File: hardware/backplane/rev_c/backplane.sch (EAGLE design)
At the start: 377 parts, among them J0 BACKPLANE_GENERIC_MODULE, J1 BACKPLANE_GENERIC_MODULE, J2 BACKPLANE_GENERIC_MODULE, J3 BACKPLANE_CONTROLLER_MODULE, J4 BACKPLANE_POWER_MODULE, J5 BACKPLANE_GENERIC_MODULE, J6 BACKPLANE_GENERIC_MODULE, J7 BACKPLANE_GENERIC_MODULE, U1 TUSB2077A, U10 SN74LVC2T45, U11 SN74LVC2T45, U12 SN74LVC2T45, U13 SN74LVC2T45, U14 SN74LVC2T45, U15 SN74LVC2T45, U16 SN74LVC2T45, U17 SN74LVC2T45, U18 SN74LVC2T45, U19 SN74LVC2T45, U2 FXMA2102, U20 TS3USB30E, U21 TS3USB30E, U22 TS3USB30E, U23 TS3USB30E, U24 TS3USB30E, U25 TS3USB30E, U26 MCP23008, U27 MCP23008, U28 MCP23008, U29 MCP23008, U3 FXMA2102, U30 MCP23008, U31 MCP23008, U4 FXMA2102, U5 FXMA2102, U6 FXMA2102, U7 FXMA2102, U8 SN74LVC2T45, U9 SN74LVC2T45, Y1 ABMM

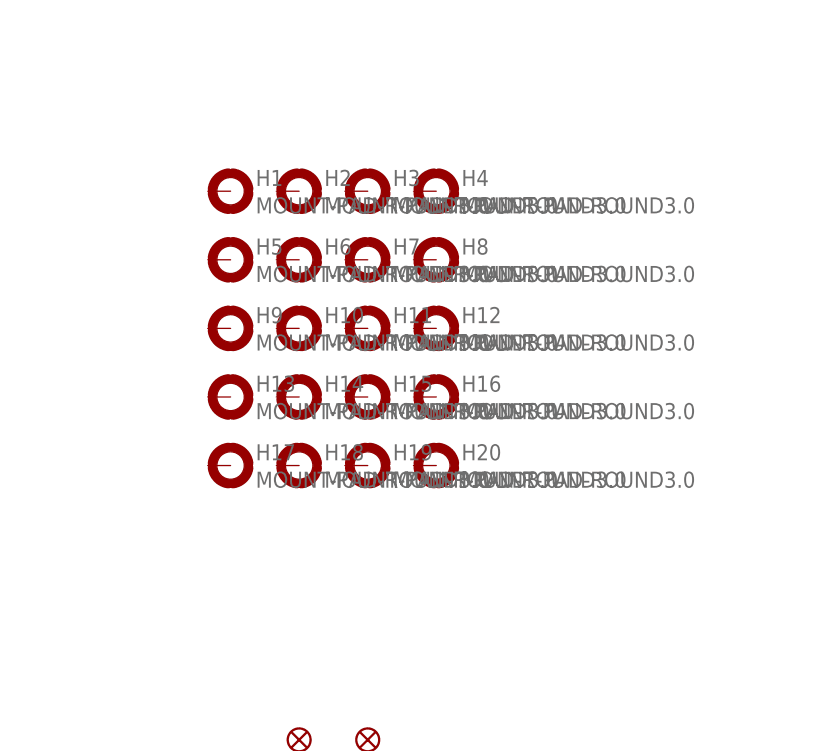
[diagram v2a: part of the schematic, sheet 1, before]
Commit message: backplane: attach mounting holes to GND
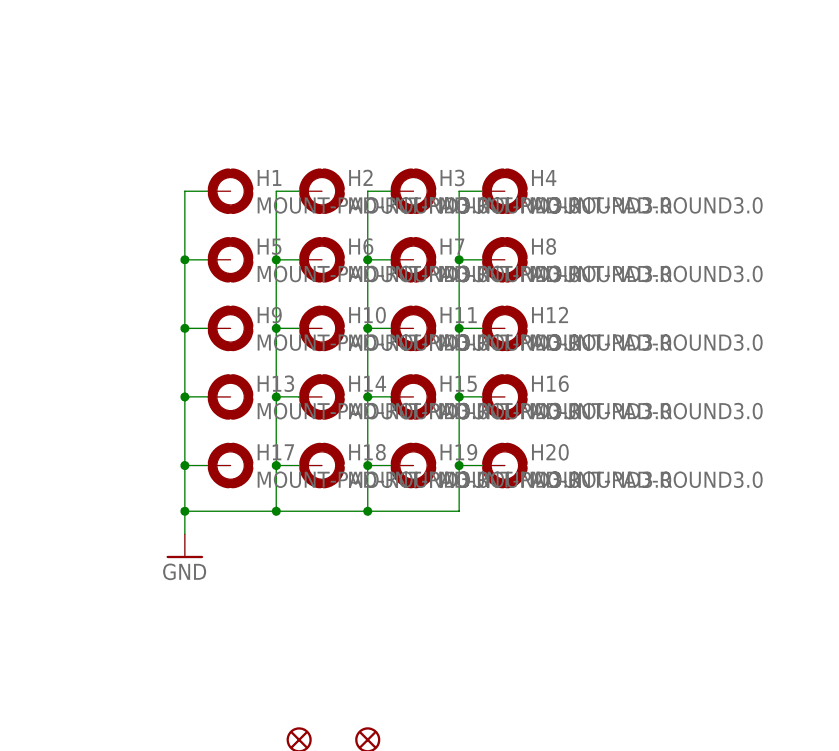
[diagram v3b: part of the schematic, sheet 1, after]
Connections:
- net GND: now also H1.MOUNT, H10.MOUNT, H11.MOUNT, H12.MOUNT, H13.MOUNT, H14.MOUNT, H15.MOUNT, H16.MOUNT, H17.MOUNT, H18.MOUNT, H19.MOUNT, H2.MOUNT, H20.MOUNT, H3.MOUNT, H4.MOUNT, H5.MOUNT, H6.MOUNT, H7.MOUNT, H8.MOUNT, H9.MOUNT
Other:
- moved on the sheet: H10, H11, H12, H14, H15, H16, H18, H19, H2, H20, H3, H4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
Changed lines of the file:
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@@
 <part name="H19" library="holes" deviceset="MOUNT-PAD-ROUND" device="3.0"/>
 <part name="H20" library="holes" deviceset="MOUNT-PAD-ROUND" device="3.0"/>
+<part name="GND72" library="umich" deviceset="GND" device=""/>
 </parts>
 <sheets>
@@
 <text x="246.38" y="182.88" size="5.08" layer="98" align="top-right">Special Modules</text>
 <text x="147.32" y="175.26" size="2.54" layer="98" align="center">Pull-up/downs</text>
-<wire x1="243.84" y1="76.2" x2="203.2" y2="76.2" width="0.6096" layer="98"/>
-<wire x1="203.2" y1="76.2" x2="203.2" y2="20.32" width="0.6096" layer="98"/>
+<wire x1="248.92" y1="76.2" x2="198.12" y2="76.2" width="0.6096" layer="98"/>
+<wire x1="198.12" y1="76.2" x2="198.12" y2="20.32" width="0.6096" layer="98"/>
 <text x="220.98" y="71.12" size="2.54" layer="98" align="center">Fiducials</text>
-<wire x1="203.2" y1="132.08" x2="203.2" y2="76.2" width="0.6096" layer="98"/>
+<wire x1="198.12" y1="132.08" x2="198.12" y2="76.2" width="0.6096" layer="98"/>
 <text x="223.52" y="129.54" size="2.54" layer="98" align="center">Plated Mounting Holes</text>
 </plain>
@@
 <instance part="JP6" gate="G$1" x="223.52" y="40.64"/>
 <instance part="H1" gate="G$1" x="208.28" y="121.92"/>
-<instance part="H2" gate="G$1" x="215.9" y="121.92"/>
-<instance part="H3" gate="G$1" x="223.52" y="121.92"/>
-<instance part="H4" gate="G$1" x="231.14" y="121.92"/>
+<instance part="H2" gate="G$1" x="218.44" y="121.92"/>
+<instance part="H3" gate="G$1" x="228.6" y="121.92"/>
+<instance part="H4" gate="G$1" x="238.76" y="121.92"/>
 <instance part="H5" gate="G$1" x="208.28" y="114.3"/>
-<instance part="H6" gate="G$1" x="215.9" y="114.3"/>
-<instance part="H7" gate="G$1" x="223.52" y="114.3"/>
-<instance part="H8" gate="G$1" x="231.14" y="114.3"/>
+<instance part="H6" gate="G$1" x="218.44" y="114.3"/>
+<instance part="H7" gate="G$1" x="228.6" y="114.3"/>
+<instance part="H8" gate="G$1" x="238.76" y="114.3"/>
 <instance part="H9" gate="G$1" x="208.28" y="106.68"/>
-<instance part="H10" gate="G$1" x="215.9" y="106.68"/>
-<instance part="H11" gate="G$1" x="223.52" y="106.68"/>
-<instance part="H12" gate="G$1" x="231.14" y="106.68"/>
+<instance part="H10" gate="G$1" x="218.44" y="106.68"/>
+<instance part="H11" gate="G$1" x="228.6" y="106.68"/>
+<instance part="H12" gate="G$1" x="238.76" y="106.68"/>
 <instance part="H13" gate="G$1" x="208.28" y="99.06"/>
-<instance part="H14" gate="G$1" x="215.9" y="99.06"/>
-<instance part="H15" gate="G$1" x="223.52" y="99.06"/>
-<instance part="H16" gate="G$1" x="231.14" y="99.06"/>
+<instance part="H14" gate="G$1" x="218.44" y="99.06"/>
+<instance part="H15" gate="G$1" x="228.6" y="99.06"/>
+<instance part="H16" gate="G$1" x="238.76" y="99.06"/>
 <instance part="H17" gate="G$1" x="208.28" y="91.44"/>
-<instance part="H18" gate="G$1" x="215.9" y="91.44"/>
-<instance part="H19" gate="G$1" x="223.52" y="91.44"/>
-<instance part="H20" gate="G$1" x="231.14" y="91.44"/>
+<instance part="H18" gate="G$1" x="218.44" y="91.44"/>
+<instance part="H19" gate="G$1" x="228.6" y="91.44"/>
+<instance part="H20" gate="G$1" x="238.76" y="91.44"/>
+<instance part="GND72" gate="1" x="203.2" y="81.28"/>
 </instances>
 <busses>
@@
 <wire x1="88.9" y1="99.06" x2="88.9" y2="93.98" width="0.1524" layer="91"/>
 </segment>
-</net>
+<segment>
+<pinref part="H17" gate="G$1" pin="MOUNT"/>
+<wire x1="205.74" y1="91.44" x2="203.2" y2="91.44" width="0.1524" layer="91"/>
+<wire x1="203.2" y1="91.44" x2="203.2" y2="86.36" width="0.1524" layer="91"/>
+<pinref part="GND72" gate="1" pin="GND"/>
+<pinref part="H13" gate="G$1" pin="MOUNT"/>
+<wire x1="203.2" y1="86.36" x2="203.2" y2="83.82" width="0.1524" layer="91"/>
+<wire x1="205.74" y1="99.06" x2="203.2" y2="99.06" width="0.1524" layer="91"/>
+<wire x1="203.2" y1="99.06" x2="203.2" y2="91.44" width="0.1524" layer="91"/>
+<junction x="203.2" y="91.44"/>
+<pinref part="H9" gate="G$1" pin="MOUNT"/>
+<wire x1="205.74" y1="106.68" x2="203.2" y2="106.68" width="0.1524" layer="91"/>
+<wire x1="203.2" y1="106.68" x2="203.2" y2="99.06" width="0.1524" layer="91"/>
+<junction x="203.2" y="99.06"/>
+<pinref part="H5" gate="G$1" pin="MOUNT"/>
+<wire x1="205.74" y1="114.3" x2="203.2" y2="114.3" width="0.1524" layer="91"/>
+<wire x1="203.2" y1="114.3" x2="203.2" y2="106.68" width="0.1524" layer="91"/>
+<junction x="203.2" y="106.68"/>
+<pinref part="H1" gate="G$1" pin="MOUNT"/>
+<wire x1="205.74" y1="121.92" x2="203.2" y2="121.92" width="0.1524" layer="91"/>
+<wire x1="203.2" y1="121.92" x2="203.2" y2="114.3" width="0.1524" layer="91"/>
+<junction x="203.2" y="114.3"/>
+<pinref part="H20" gate="G$1" pin="MOUNT"/>
+<wire x1="236.22" y1="91.44" x2="233.68" y2="91.44" width="0.1524" layer="91"/>
+<wire x1="233.68" y1="91.44" x2="233.68" y2="86.36" width="0.1524" layer="91"/>
+<wire x1="233.68" y1="86.36" x2="223.52" y2="86.36" width="0.1524" layer="91"/>
+<junction x="203.2" y="86.36"/>
+<pinref part="H16" gate="G$1" pin="MOUNT"/>
+<wire x1="223.52" y1="86.36" x2="213.36" y2="86.36" width="0.1524" layer="91"/>
+<wire x1="213.36" y1="86.36" x2="203.2" y2="86.36" width="0.1524" layer="91"/>
+<wire x1="236.22" y1="99.06" x2="233.68" y2="99.06" width="0.1524" layer="91"/>
+<wire x1="233.68" y1="99.06" x2="233.68" y2="91.44" width="0.1524" layer="91"/>
+<junction x="233.68" y="91.44"/>
+<pinref part="H12" gate="G$1" pin="MOUNT"/>
+<wire x1="236.22" y1="106.68" x2="233.68" y2="106.68" width="0.1524" layer="91"/>
+<wire x1="233.68" y1="106.68" x2="233.68" y2="99.06" width="0.1524" layer="91"/>
+<junction x="233.68" y="99.06"/>
+<pinref part="H8" gate="G$1" pin="MOUNT"/>
+<wire x1="236.22" y1="114.3" x2="233.68" y2="114.3" width="0.1524" layer="91"/>
+<wire x1="233.68" y1="114.3" x2="233.68" y2="106.68" width="0.1524" layer="91"/>
+<junction x="233.68" y="106.68"/>
+<pinref part="H4" gate="G$1" pin="MOUNT"/>
+<wire x1="236.22" y1="121.92" x2="233.68" y2="121.92" width="0.1524" layer="91"/>
+<wire x1="233.68" y1="121.92" x2="233.68" y2="114.3" width="0.1524" layer="91"/>
+<junction x="233.68" y="114.3"/>
+<pinref part="H18" gate="G$1" pin="MOUNT"/>
+<wire x1="215.9" y1="91.44" x2="213.36" y2="91.44" width="0.1524" layer="91"/>
+<wire x1="213.36" y1="91.44" x2="213.36" y2="86.36" width="0.1524" layer="91"/>
+<junction x="213.36" y="86.36"/>
+<pinref part="H14" gate="G$1" pin="MOUNT"/>
+<wire x1="215.9" y1="99.06" x2="213.36" y2="99.06" width="0.1524" layer="91"/>
+<wire x1="213.36" y1="99.06" x2="213.36" y2="91.44" width="0.1524" layer="91"/>
+<junction x="213.36" y="91.44"/>
+<pinref part="H10" gate="G$1" pin="MOUNT"/>
+<wire x1="215.9" y1="106.68" x2="213.36" y2="106.68" width="0.1524" layer="91"/>
+<wire x1="213.36" y1="106.68" x2="213.36" y2="99.06" width="0.1524" layer="91"/>
+<junction x="213.36" y="99.06"/>
+<pinref part="H6" gate="G$1" pin="MOUNT"/>
+<wire x1="215.9" y1="114.3" x2="213.36" y2="114.3" width="0.1524" layer="91"/>
+<wire x1="213.36" y1="114.3" x2="213.36" y2="106.68" width="0.1524" layer="91"/>
+<junction x="213.36" y="106.68"/>
+<pinref part="H2" gate="G$1" pin="MOUNT"/>
+<wire x1="215.9" y1="121.92" x2="213.36" y2="121.92" width="0.1524" layer="91"/>
+<wire x1="213.36" y1="121.92" x2="213.36" y2="114.3" width="0.1524" layer="91"/>
+<junction x="213.36" y="114.3"/>
+<pinref part="H19" gate="G$1" pin="MOUNT"/>
+<wire x1="226.06" y1="91.44" x2="223.52" y2="91.44" width="0.1524" layer="91"/>
+<wire x1="223.52" y1="91.44" x2="223.52" y2="86.36" width="0.1524" layer="91"/>
+<junction x="223.52" y="86.36"/>
+<pinref part="H15" gate="G$1" pin="MOUNT"/>
+<wire x1="226.06" y1="99.06" x2="223.52" y2="99.06" width="0.1524" layer="91"/>
+<wire x1="223.52" y1="99.06" x2="223.52" y2="91.44" width="0.1524" layer="91"/>
+<junction x="223.52" y="91.44"/>
+<pinref part="H11" gate="G$1" pin="MOUNT"/>
+<wire x1="226.06" y1="106.68" x2="223.52" y2="106.68" width="0.1524" layer="91"/>
+<wire x1="223.52" y1="106.68" x2="223.52" y2="99.06" width="0.1524" layer="91"/>
+<junction x="223.52" y="99.06"/>
+<pinref part="H7" gate="G$1" pin="MOUNT"/>
+<wire x1="226.06" y1="114.3" x2="223.52" y2="114.3" width="0.1524" layer="91"/>
+<wire x1="223.52" y1="114.3" x2="223.52" y2="106.68" width="0.1524" layer="91"/>
+<junction x="223.52" y="106.68"/>
+<pinref part="H3" gate="G$1" pin="MOUNT"/>
+<wire x1="226.06" y1="121.92" x2="223.52" y2="121.92" width="0.1524" layer="91"/>
+<wire x1="223.52" y1="121.92" x2="223.52" y2="114.3" width="0.1524" layer="91"/>
+<junction x="223.52" y="114.3"/>
+</segment>
+</net>

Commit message: backplane: smaller gpio extender package
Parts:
- U26, U27, U28, U29, U30, U31: value MCP23008 -> MCP23008QFN; device signpost:MCP23008 -> signpost:MCP23008QFN
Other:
- moved on the sheet: U26, U27, U28, U29, U30, U31

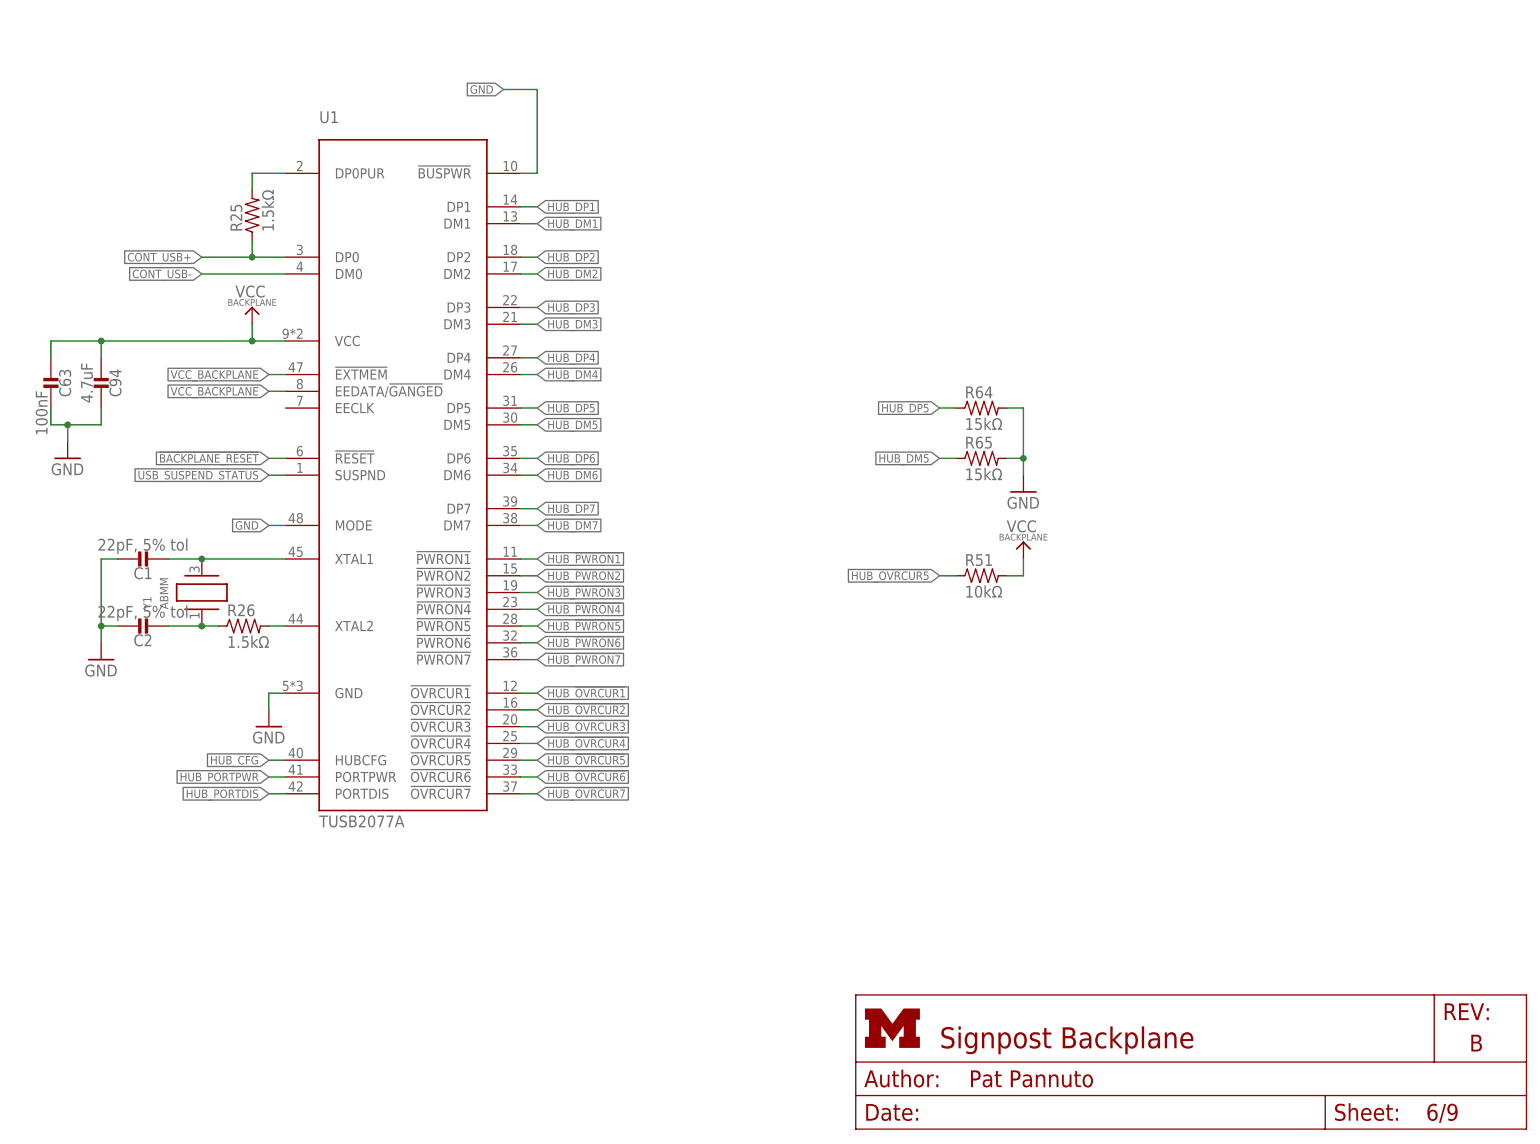
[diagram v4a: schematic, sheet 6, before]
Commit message: backplane: add gpio extender for usb signals
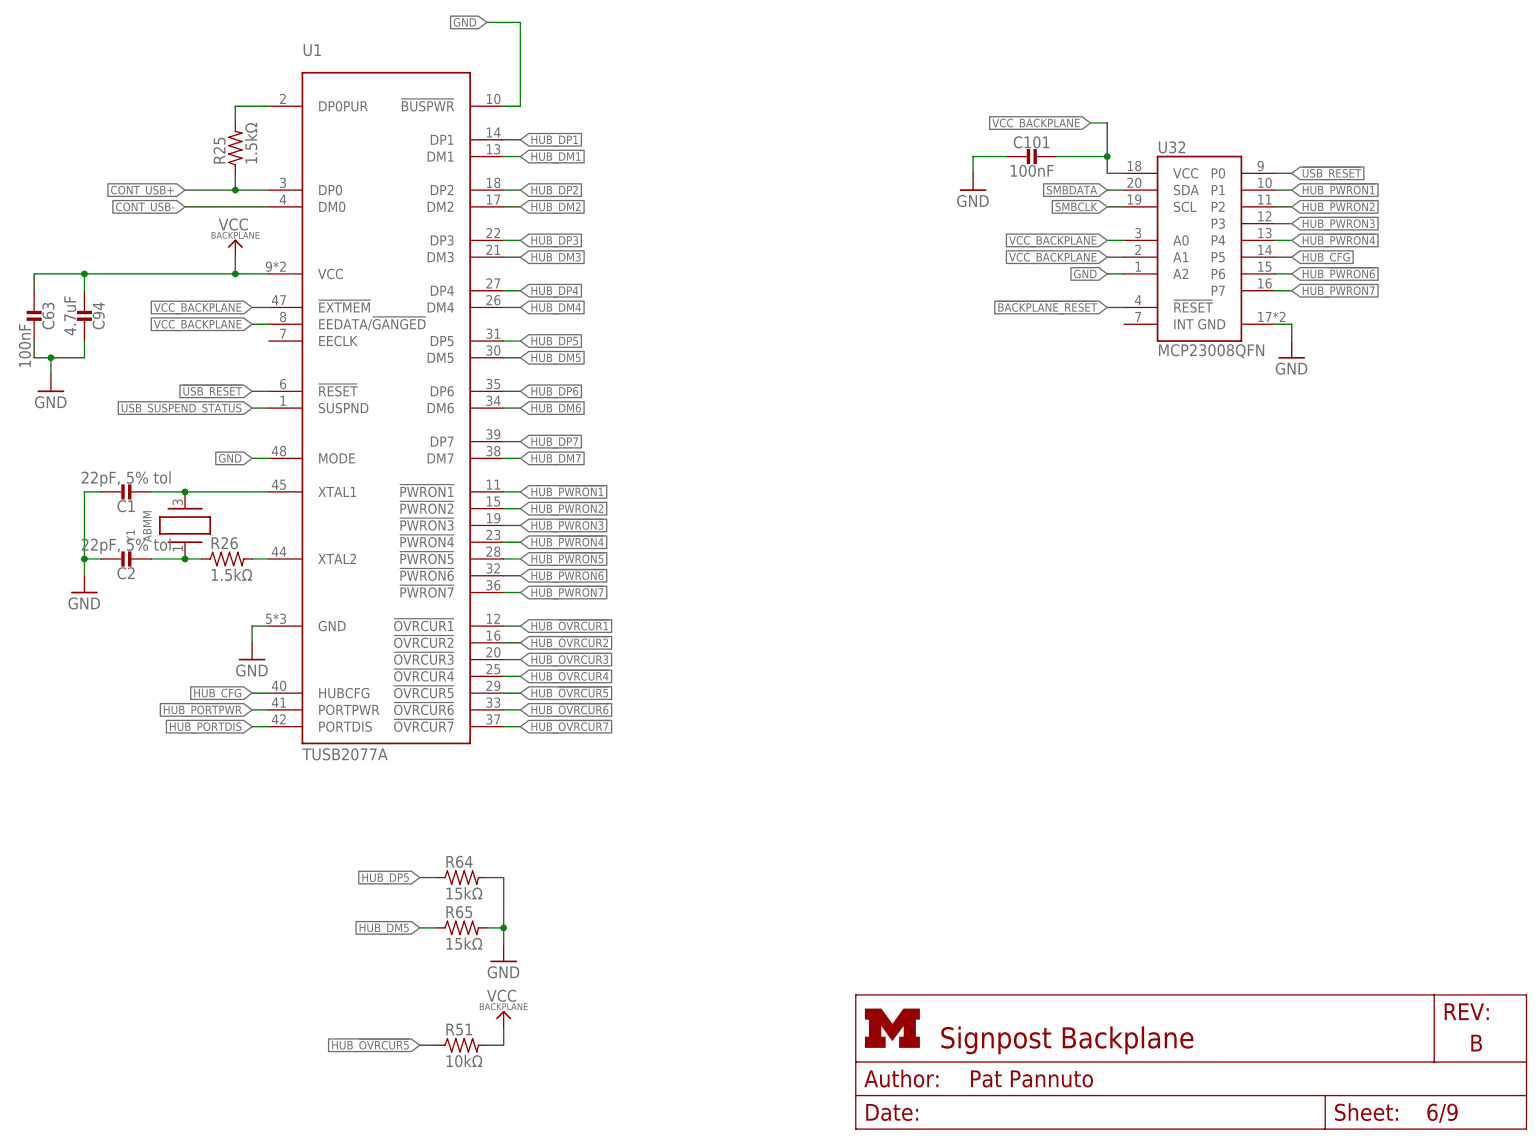
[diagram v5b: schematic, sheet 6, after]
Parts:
- added C101: 100nF, passives:CAPACITOR0603_CAP
- added U32: MCP23008QFN, signpost:MCP23008QFN
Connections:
- new net !USB_RESET: U1.!RESET, U32.P0
- net !BACKPLANE_RESET: now also U32.!RESET; no longer U1.!RESET
- net GND: now also C101.2, U32.A2, U32.GND
- net HUB_!PWRON1: now also U32.P1
- net HUB_!PWRON2: now also U32.P2
- net HUB_!PWRON3: now also U32.P3
- net HUB_!PWRON4: now also U32.P4
- net HUB_!PWRON6: now also U32.P6
- net HUB_!PWRON7: now also U32.P7
- net HUB_CFG: now also U32.P5
- net SMBCLK: now also U32.SCL
- net SMBDATA: now also U32.SDA
- net VCC_BACKPLANE: now also C101.1, U32.A0, U32.A1, U32.VCC
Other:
- note added: "--> Mod0"
- note added: "--> Mod1"
- note added: "--> Mod2"
- note added: "--> Mod5"
- note added: "--> Mod6"
- note added: "--> Mod7"
- note added: "Addr 3"
- note added: "HUBCFG: Hub configured. When the hub is configured, HUBCFG is high. When the hub is not configured, HUBCFG is low."
- note added: "Hub Monitoring and Reset The !PWRON! signal for each used port is wired to the matching pin on the GPIO extender. The hub will automatically disable power to a port if the !OVRCUR! signal activates for any port. As port 5 is currently unused, the HUBCFG status line is wired to that port, however when we integrate the power module into the backplane that will likely shift to montoring !PWRON! for 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"
- note added: "Note: An additional GPIO extender found on the USB sheet consumes address 3 (the controller slot) to facilitate run-time reset and monitoring of USB status"
- note added: "PORTDIS: LED indicator control When no port is disabled, PORTDIS is high. When any port is disabled, PORTDIS is low."
- note added: "PORTPWR: Any port powered. When any port is powered on, PORTPWR is high. When all ports are off, PORTPWR is low."
- moved on the sheet: C1, C2, C63, C94, R25, R26, R51, R64, R65, U1, Y1
